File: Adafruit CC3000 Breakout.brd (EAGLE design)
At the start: 39.4 x 59.7 mm, 33 parts, among them IC1 ATmega1284P, U1 CC3000MOD, X1 2500AT44M0400E

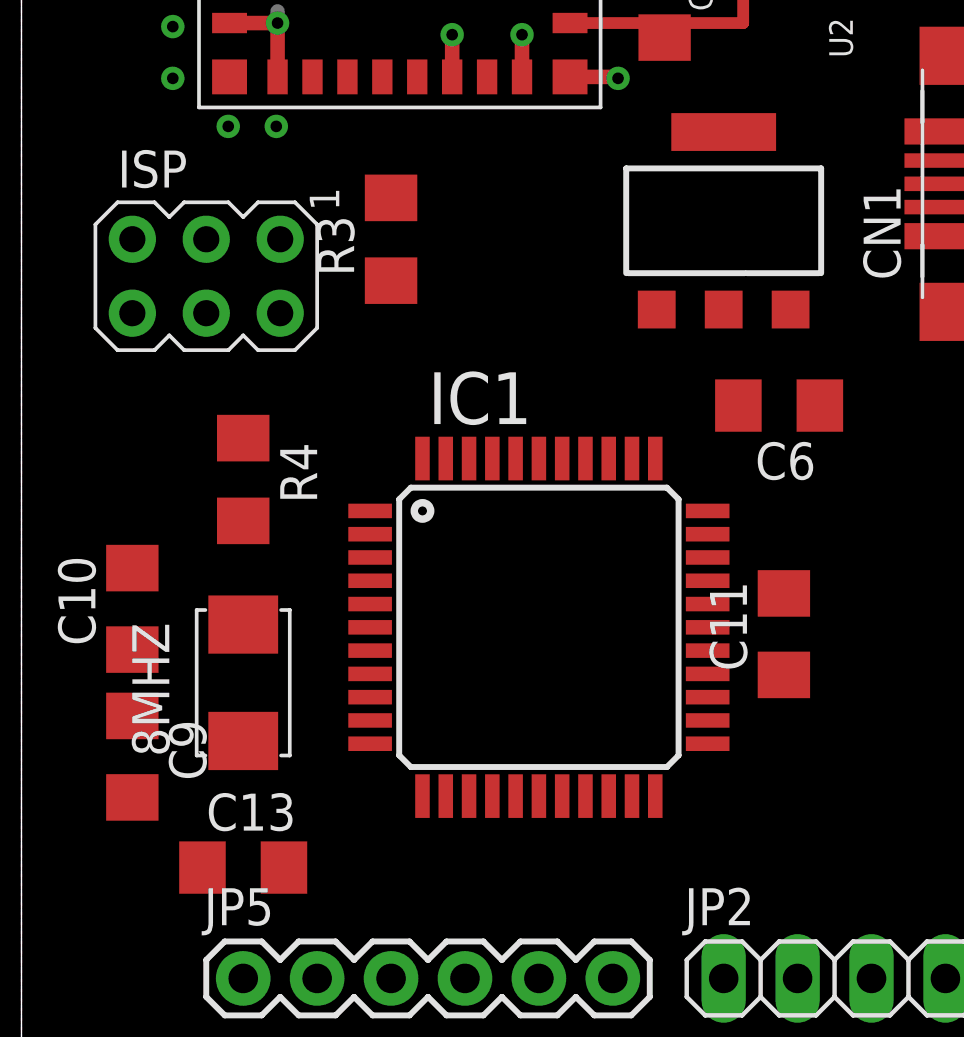
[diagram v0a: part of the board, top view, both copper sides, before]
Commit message: Make some ground via's.
In the hopes it will help with routing.
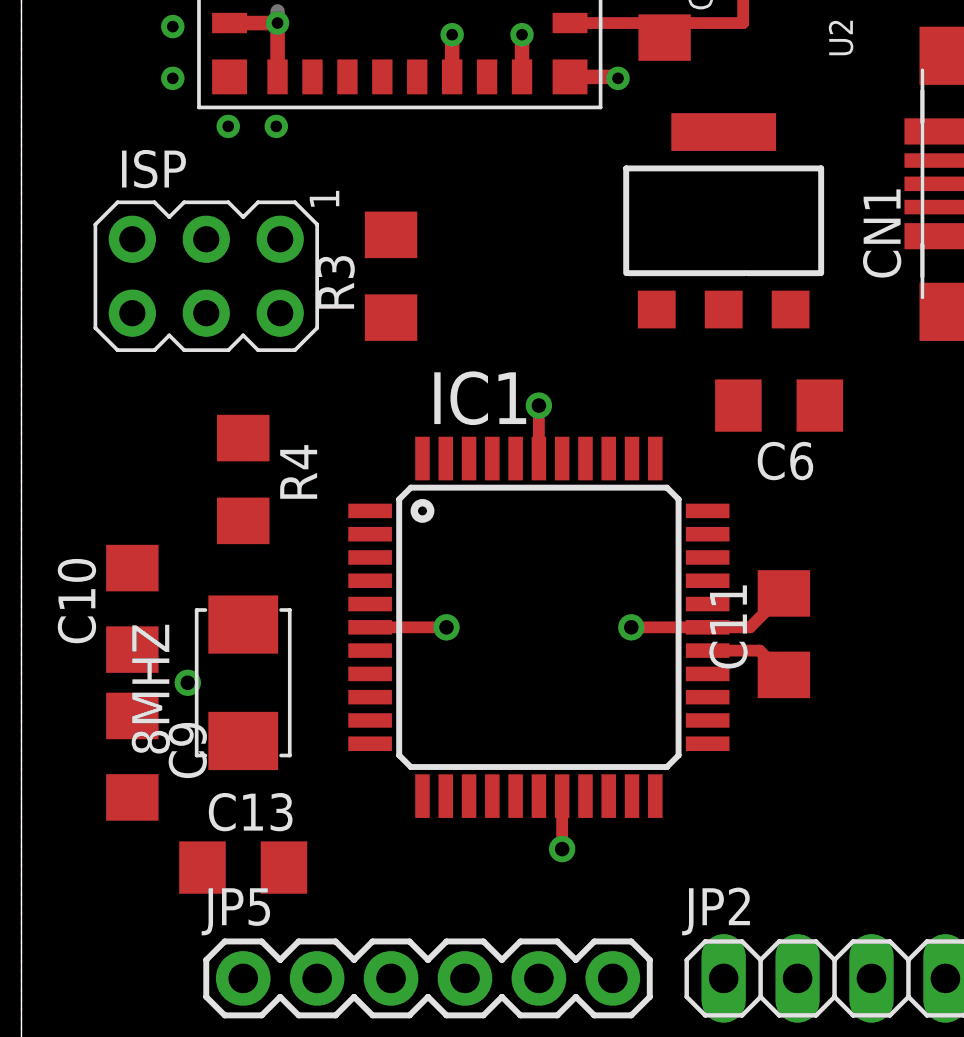
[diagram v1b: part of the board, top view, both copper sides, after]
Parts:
- moved R3 1.27 mm to (12.7, 26.7)
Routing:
- net GND: track 47.9 -> 59.9 mm, vias 51 -> 56
- net VBAT: track 17.6 -> 20.6 mm
